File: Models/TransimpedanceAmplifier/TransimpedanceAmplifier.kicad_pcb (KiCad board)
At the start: 2 copper layers, 107 parts, among them J1 Conn_01x02_Socket, J10 Conn_01x02_Pin, J11 Conn_01x24_Socket, J14 Conn_01x24_Socket, J2 Conn_01x02_Socket, J3 Conn_01x03_Pin, J4 Conn_01x02_Pin, J5 Conn_01x02_Pin, J6 Conn_01x02_Pin, J7 Conn_01x02_Pin, J8 Conn_01x02_Pin, J9 Conn_01x02_Pin, Q1 Q_PNP, Q2 Q_NPN, U1 LM7905, -5V, 5%, U10 DAC81401, U11 ISO7641FM, U12 ISO7641FM, U13 ADS8699, U2 LM7805, 5V, 5%, U3 OPA828, U4 AD8615, U5 OP37GPZ, U6 LM7915, -15V, 5%, U7 LM7815, 15V, 5%, U8 LM7805, 5V, 5%, U9 TLV76133, 3.3V, 1%

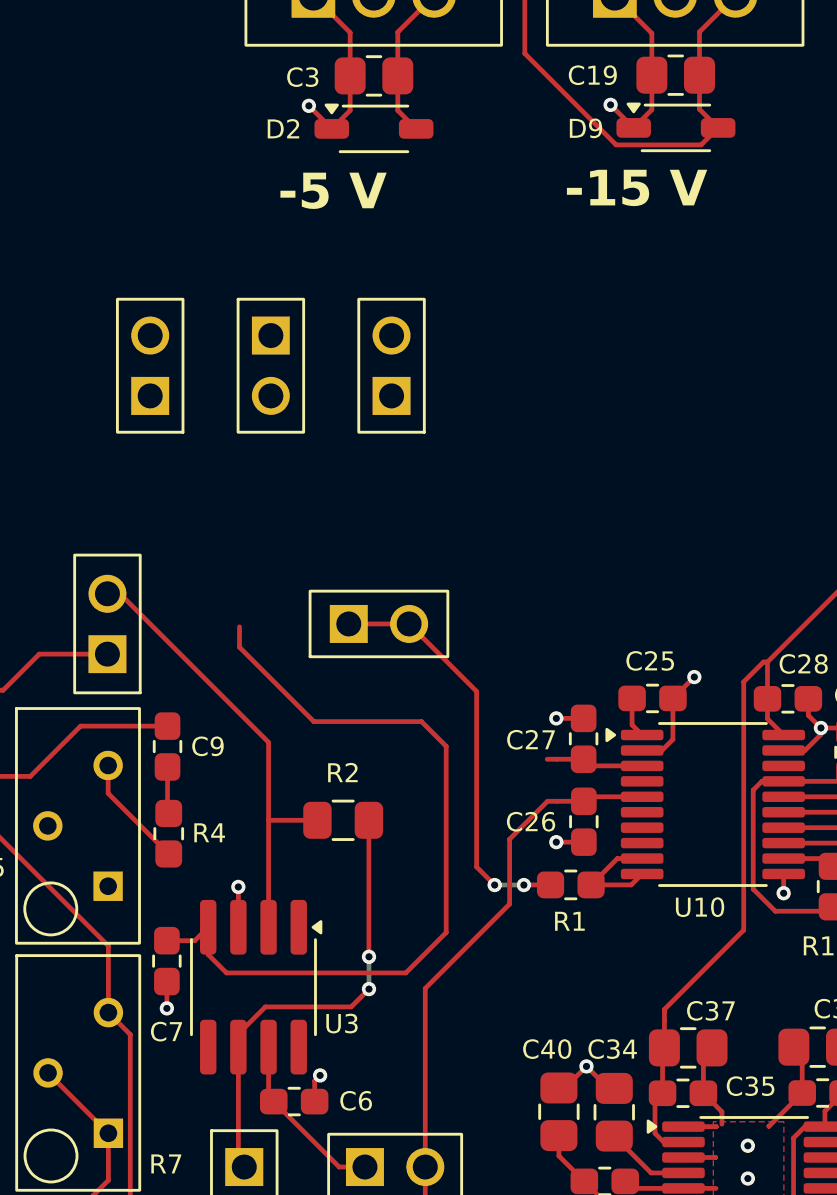
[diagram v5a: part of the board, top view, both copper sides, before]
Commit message: Rewired the -15 V power trace
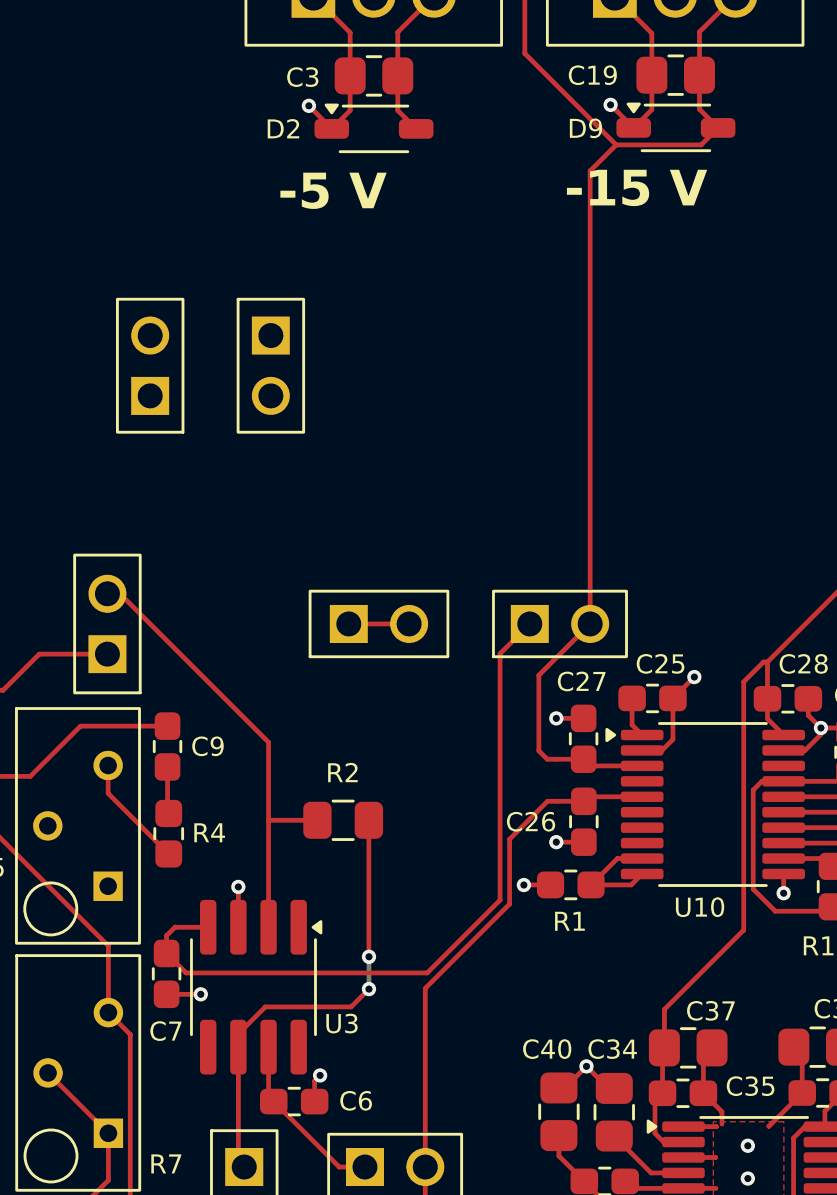
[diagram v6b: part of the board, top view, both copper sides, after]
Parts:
- moved J5 13.0 mm to (116.5, 85.7), turned to 90 degrees
- moved C7 0.54 mm to (100.0, 100.4)
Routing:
- net /-15V: track 155.3 -> 182.7 mm
- net Net-(J1-Pin_1): track 17.4 -> 3.66 mm, vias 2 -> 1
- net /TIA_OneStage/V-: track 33.3 -> 30.4 mm
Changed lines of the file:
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@@
 	(footprint "Connector_Custom:PinHeader_1x2"
 		(layer "F.Cu")
-		(at 109.46 74.79 180)
+		(at 116.55 85.66 90)
 		(property "Reference" "J5"
-			(at 0.0025 -3.5625 180)
+			(at 0.0025 -3.5625 90)
 			(unlocked yes)
 			(layer "F.SilkS")
@@
 		)
 		(property "Value" "Conn_01x02_Pin"
-			(at 0.0025 -2.3625 180)
+			(at 0.0025 -2.3625 90)
 			(unlocked yes)
 			(layer "F.Fab")
@@
 		)
 		(property "Datasheet" "~"
-			(at 0 0 180)
+			(at 0 0 90)
 			(unlocked yes)
 			(layer "F.Fab")
@@
 		)
 		(property "Description" "Generic connector, single row, 01x02, script generated"
-			(at 0 0 180)
+			(at 0 0 90)
 			(unlocked yes)
 			(layer "F.Fab")
@@
 		)
 		(property "Purchase Link" "https://www.digikey.com/en/products/detail/sullins-connector-solutions/QPC02SXGN-RC/2618262"
-			(at 0 0 180)
+			(at 0 0 90)
 			(unlocked yes)
 			(layer "F.Fab")
@@
 		)
 		(property "Cost" "$0.10"
-			(at 0 0 180)
+			(at 0 0 90)
 			(unlocked yes)
 			(layer "F.Fab")
@@
 		)
 		(property "RoHS Compliant" "YES"
-			(at 0 0 180)
+			(at 0 0 90)
 			(unlocked yes)
 			(layer "F.Fab")
@@
 		)
 		(property "Cost (qty10)" "$0.025"
-			(at 0 0 180)
+			(at 0 0 90)
 			(unlocked yes)
 			(layer "F.Fab")
@@
 		)
 		(fp_text user "${REFERENCE}"
-			(at 0.0025 -1.1625 180)
+			(at 0.0025 -1.1625 90)
 			(unlocked yes)
 			(layer "F.Fab")
@@
 		)
 		(pad "1" thru_hole rect
-			(at 0 -1.27 180)
+			(at 0 -1.27 90)
 			(size 1.6 1.6)
 			(drill 1.05)
@@
 		)
 		(pad "2" thru_hole circle
-			(at 0 1.27 180)
+			(at 0 1.27 90)
 			(size 1.6 1.6)
 			(drill 1.05)
@@
 	)
 	(footprint "TwoTerminal:CAPC0603"
-		(locked yes)
 		(layer "F.Cu")
 		(at 117.545 90.495 90)
 		(property "Reference" "C27"
-			(at -0.07 -2.2 0)
+			(at 2.385 -0.065 0)
 			(unlocked yes)
 			(layer "F.SilkS")
@@
 		(at 120.445 88.795)
 		(property "Reference" "C25"
-			(at -0.08 -1.55 0)
+			(at 0.355 -1.425 0)
 			(unlocked yes)
 			(layer "F.SilkS")
@@
 	)
 	(footprint "TwoTerminal:CAPC0603"
-		(locked yes)
 		(layer "F.Cu")
-		(at 100.002501 99.8525 -90)
+		(at 99.99 100.39 -90)
 		(property "Reference" "C7"
-			(at 2.9975 0 0)
+			(at 2.4375 0.012501 0)
 			(unlocked yes)
 			(layer "F.SilkS")
@@
 	)
 	(segment
+		(start 99.99 101.25)
+		(end 101.43 101.25)
+		(width 0.2)
+		(layer "F.Cu")
+		(net 5)
+	)
+	(segment
 		(start 85.87 97.890001)
 		(end 84.9 96.920001)
@@
 	)
 	(segment
-		(start 100.002501 100.7125)
-		(end 100.002501 101.8425)
-		(width 0.2)
-		(layer "F.Cu")
-		(net 5)
-	)
-	(segment
 		(start 121.1 123.86)
 		(end 121.1 122.7675)
@@
 	)
 	(via
-		(at 100.002501 101.8425)
-		(size 0.6)
-		(drill 0.3)
-		(layers "F.Cu" "B.Cu")
-		(net 5)
-	)
-	(via
 		(at 141.14 58.96)
 		(size 0.6)
@@
 		(net 5)
 	)
+	(via
+		(at 101.43 101.25)
+		(size 0.6)
+		(drill 0.3)
+		(layers "F.Cu" "B.Cu")
+		(net 5)
+	)
 	(segment
 		(start 131.3975 90.745)
@@
 	)
 	(segment
+		(start 117.82 85.66)
+		(end 117.82 66.590872)
+		(width 0.2)
+		(layer "F.Cu")
+		(net 13)
+	)
+	(segment
 		(start 75.94 107.67)
 		(end 75.94 59.4)
@@
 	)
 	(segment
+		(start 115.66 87.82)
+		(end 117.82 85.66)
+		(width 0.2)
+		(layer "F.Cu")
+		(net 13)
+	)
+	(segment
 		(start 122.4225 62.56)
 		(end 122.4225 63.99375)
@@
 	)
 	(segment
+		(start 117.82 66.590872)
+		(end 118.916122 65.49475)
+		(width 0.2)
+		(layer "F.Cu")
+		(net 13)
+	)
+	(segment
+		(start 115.66 91)
+		(end 115.66 87.82)
+		(width 0.2)
+		(layer "F.Cu")
+		(net 13)
+	)
+	(segment
 		(start 108.3325 54.73)
 		(end 108.3325 53.0775)
@@
 	)
 	(segment
+		(start 116.015 91.355)
+		(end 115.66 91)
+		(width 0.2)
+		(layer "F.Cu")
+		(net 13)
+	)
+	(segment
 		(start 89.600833 129.051)
 		(end 81.694139 129.051)
@@
 	)
 	(segment
-		(start 102.512501 100.35)
-		(end 110.06 100.35)
+		(start 100.81 100.35)
+		(end 110.9629 100.35)
 		(width 0.2)
 		(layer "F.Cu")
@@
 	)
 	(segment
-		(start 111.76 90.81)
-		(end 110.72 89.77)
+		(start 114.028 86.912)
+		(end 115.28 85.66)
 		(width 0.2)
 		(layer "F.Cu")
@@
 	)
 	(segment
-		(start 106.19 89.77)
-		(end 103.06 86.64)
+		(start 100.35 98.42)
+		(end 99.99 98.78)
 		(width 0.2)
 		(layer "F.Cu")
@@
 	)
 	(segment
-		(start 100.002501 98.9925)
-		(end 101.1775 98.9925)
+		(start 110.9629 100.35)
+		(end 114.028 97.2849)
 		(width 0.2)
 		(layer "F.Cu")
@@
 	)
 	(segment
-		(start 101.7425 99.579999)
-		(end 102.512501 100.35)
+		(start 100.3575 98.4275)
+		(end 100.35 98.42)
 		(width 0.2)
 		(layer "F.Cu")
@@
 	)
 	(segment
-		(start 103.06 86.64)
-		(end 103.06 85.78)
+		(start 99.99 99.53)
+		(end 100.81 100.35)
 		(width 0.2)
 		(layer "F.Cu")
@@
 	)
 	(segment
-		(start 101.1775 98.9925)
-		(end 101.7425 98.4275)
+		(start 114.028 97.2849)
+		(end 114.028 86.912)
 		(width 0.2)
 		(layer "F.Cu")
@@
 	)
 	(segment
-		(start 111.76 98.65)
-		(end 111.76 90.81)
+		(start 99.99 98.78)
+		(end 99.99 99.53)
 		(width 0.2)
 		(layer "F.Cu")
@@
 	(segment
 		(start 101.7425 98.4275)
-		(end 101.7425 99.579999)
-		(width 0.2)
-		(layer "F.Cu")
-		(net 15)
-	)
-	(segment
-		(start 110.72 89.77)
-		(end 106.19 89.77)
-		(width 0.2)
-		(layer "F.Cu")
-		(net 15)
-	)
-	(segment
-		(start 110.06 100.35)
-		(end 111.76 98.65)
+		(end 100.3575 98.4275)
 		(width 0.2)
 		(layer "F.Cu")
@@
 	)
 	(segment
-		(start 113.04 88.5)
-		(end 110.2 85.66)
-		(width 0.2)
-		(layer "F.Cu")
-		(net 47)
-	)
-	(segment
-		(start 113.04 95.89)
-		(end 113.04 88.5)
-		(width 0.2)
-		(layer "F.Cu")
-		(net 47)
-	)
-	(segment
-		(start 113.8 96.65)
-		(end 113.04 95.89)
-		(width 0.2)
-		(layer "F.Cu")
-		(net 47)
-	)
-	(segment
 		(start 116.1525 96.645)
 		(end 115.035 96.645)
@@
 	)
 	(via
-		(at 113.8 96.65)
-		(size 0.6)
-		(drill 0.3)
-		(layers "F.Cu" "B.Cu")
-		(net 47)
-	)
-	(via
 		(at 115.03 96.65)
 		(size 0.6)
@@
 		(net 47)
 	)
-	(segment
-		(start 115.03 96.65)
-		(end 113.8 96.65)
-		(width 0.2)
-		(layer "B.Cu")
-		(net 47)
-	)

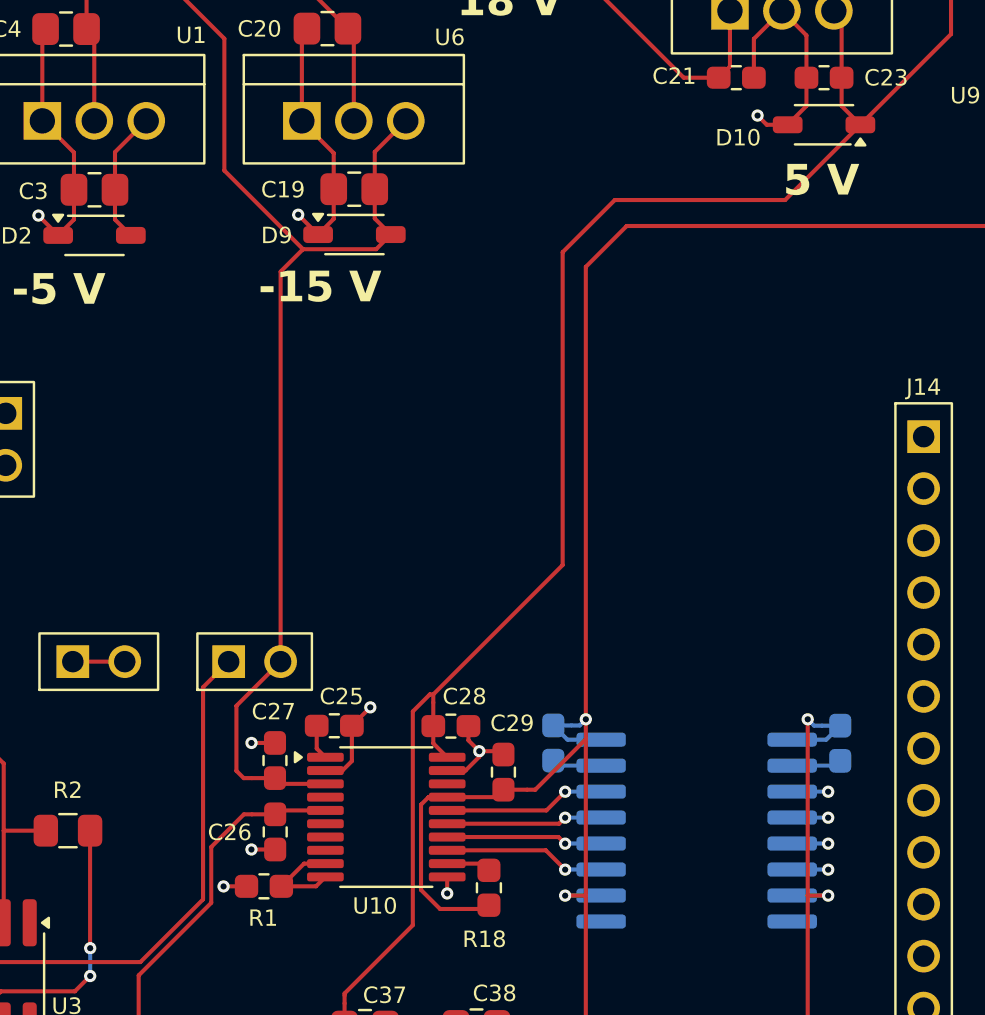
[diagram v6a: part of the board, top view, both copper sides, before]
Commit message: Locked the recently modified components
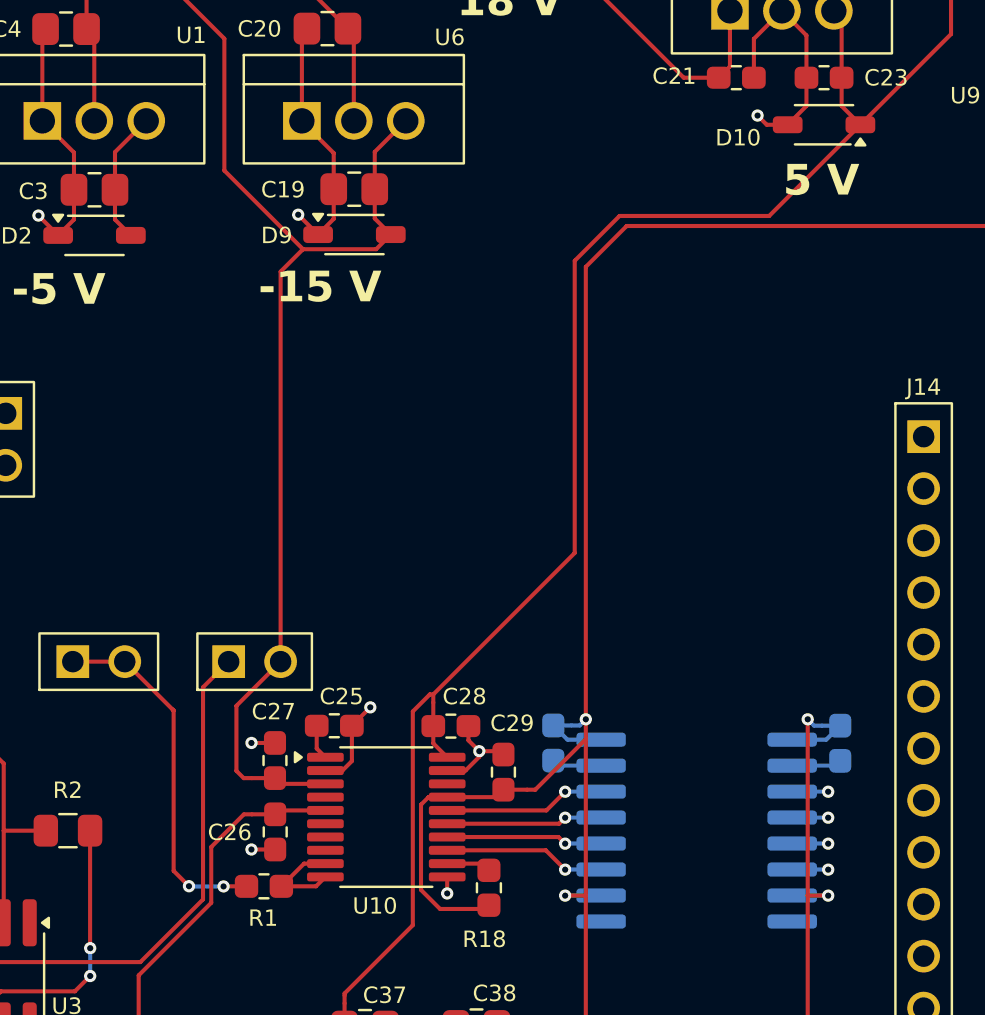
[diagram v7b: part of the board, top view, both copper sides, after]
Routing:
- net Net-(J1-Pin_1): track 3.66 -> 17.7 mm, vias 1 -> 2
- net /5V_Converter: track 81.4 -> 80.9 mm
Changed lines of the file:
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@@
 	)
 	(footprint "Connector_Custom:PinHeader_1x2"
+		(locked yes)
 		(layer "F.Cu")
 		(at 116.55 85.66 90)
@@
 	)
 	(footprint "TwoTerminal:CAPC0603"
+		(locked yes)
 		(layer "F.Cu")
 		(at 99.99 100.39 -90)
@@
 	)
 	(segment
+		(start 146.1675 59.41)
+		(end 141.7075 63.87)
+		(width 0.2)
+		(layer "F.Cu")
+		(net 24)
+	)
+	(segment
 		(start 145.25 57.11)
 		(end 145.25 54.22)
@@
 	)
 	(segment
-		(start 124.284 98.546)
-		(end 124.284 88.09569)
+		(start 134.39 63.87)
+		(end 132.2 66.06)
 		(width 0.2)
 		(layer "F.Cu")
@@
 	)
 	(segment
-		(start 131.61 65.64)
-		(end 131.61 80.93679)
+		(start 124.284 98.546)
+		(end 124.284 88.09569)
 		(width 0.2)
 		(layer "F.Cu")
@@
 	)
 	(segment
-		(start 146.1675 59.41)
-		(end 142.4875 63.09)
-		(width 0.2)
-		(layer "F.Cu")
-		(net 24)
-	)
-	(segment
 		(start 150.6 51.85)
 		(end 151.61 50.84)
@@
 	)
 	(segment
-		(start 142.4875 63.09)
-		(end 134.16 63.09)
+		(start 145.25 54.22)
+		(end 144.87 53.84)
 		(width 0.2)
 		(layer "F.Cu")
@@
 	)
 	(segment
-		(start 145.25 54.22)
-		(end 144.87 53.84)
+		(start 132.2 66.06)
+		(end 132.2 80.34679)
 		(width 0.2)
 		(layer "F.Cu")
@@
 	)
 	(segment
-		(start 155.0675 50.84)
-		(end 155.0675 52.0725)
+		(start 132.2 80.34679)
+		(end 125.285 87.26179)
 		(width 0.2)
 		(layer "F.Cu")
@@
 	)
 	(segment
-		(start 131.61 80.93679)
-		(end 125.285 87.26179)
+		(start 155.0675 50.84)
+		(end 155.0675 52.0725)
 		(width 0.2)
 		(layer "F.Cu")
@@
 	)
 	(segment
-		(start 134.16 63.09)
-		(end 131.61 65.64)
+		(start 141.7075 63.87)
+		(end 134.39 63.87)
 		(width 0.2)
 		(layer "F.Cu")
@@
 	)
 	(segment
+		(start 110.2 85.66)
+		(end 112.59 88.05)
+		(width 0.2)
+		(layer "F.Cu")
+		(net 47)
+	)
+	(segment
+		(start 112.59 88.05)
+		(end 112.53 87.99)
+		(width 0.2)
+		(layer "F.Cu")
+		(net 47)
+	)
+	(segment
 		(start 107.66 85.66)
 		(end 110.2 85.66)
@@
 		(net 47)
 	)
+	(segment
+		(start 112.59 88.05)
+		(end 112.59 95.89)
+		(width 0.2)
+		(layer "F.Cu")
+		(net 47)
+	)
+	(segment
+		(start 113.34 96.64)
+		(end 112.59 95.89)
+		(width 0.2)
+		(layer "F.Cu")
+		(net 47)
+	)
+	(via
+		(at 113.34 96.64)
+		(size 0.6)
+		(drill 0.3)
+		(layers "F.Cu" "B.Cu")
+		(net 47)
+	)
 	(via
 		(at 115.03 96.65)
@@
 		(net 47)
 	)
+	(segment
+		(start 115.03 96.65)
+		(end 113.35 96.65)
+		(width 0.2)
+		(layer "B.Cu")
+		(net 47)
+	)
+	(segment
+		(start 113.35 96.65)
+		(end 113.34 96.64)
+		(width 0.2)
+		(layer "B.Cu")
+		(net 47)
+	)

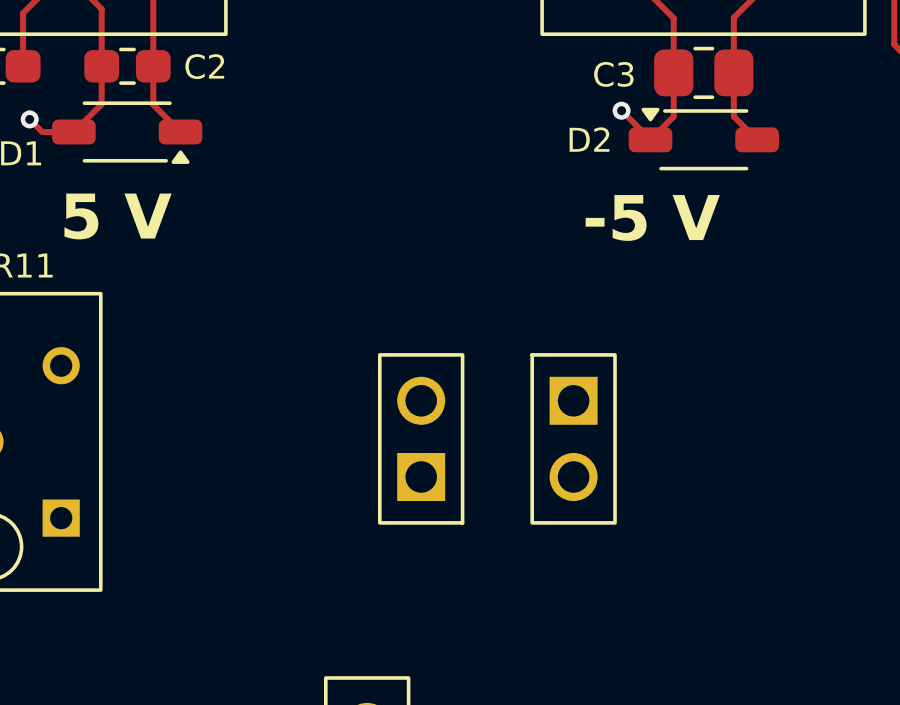
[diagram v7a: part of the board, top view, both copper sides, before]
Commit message: Fixed a bug in the schematic: the -1.5 V net was not connected to its voltage divider
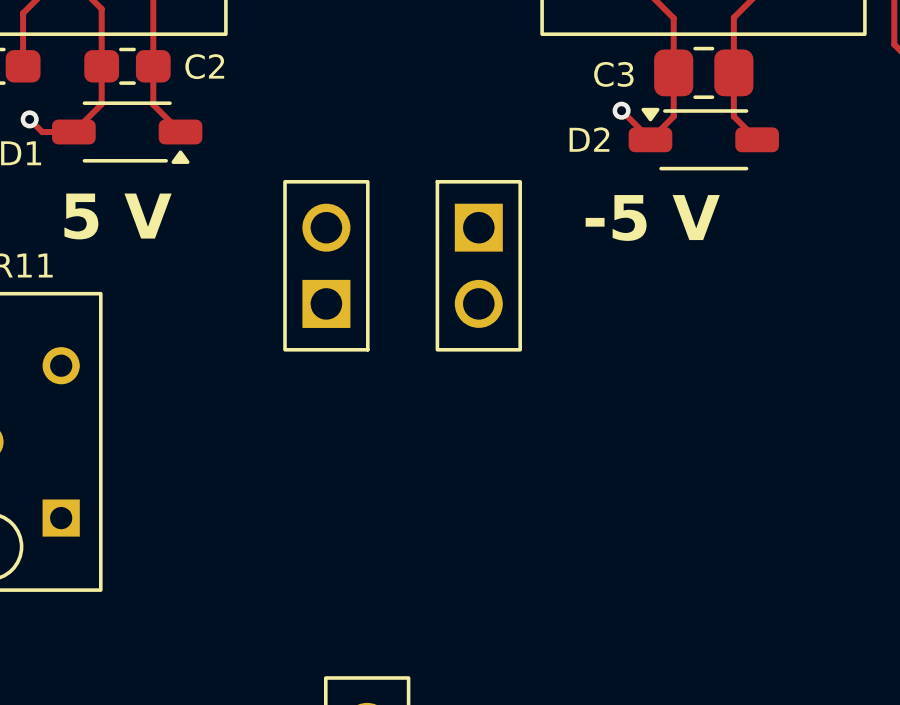
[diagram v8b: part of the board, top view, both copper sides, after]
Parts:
- moved J6 6.58 mm to (101.2, 69.0)
- moved J7 6.58 mm to (96.1, 69.0)
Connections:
- R10 pad 1: Net-(R10-Pad1) -> /TIA_TwoStage/PreAmplifier/-1.5V
- R9 pad 2: Net-(R10-Pad1) -> /TIA_TwoStage/PreAmplifier/-1.5V
